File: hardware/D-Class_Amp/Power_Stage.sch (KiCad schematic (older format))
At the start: 19 parts, among them Q301 PHP23NQ11T, Q302 PHP23NQ11T, Q303 PHP23NQ11T, Q304 PHP23NQ11T, U301 NCP1117-12_TO252, U302 IR21834, U303 IR21834

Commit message: foot
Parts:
- R301, R302, R303, R304, R305, R306: footprint (none) -> Resistor_SMD:R_0805_2012Metric_Pad1.20x1.40mm_HandSolder
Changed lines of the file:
@@
 Non-Inverting Half-Bridge\n
-$Comp
-L Device:R R305
-U 1 1 610540BF
-P 5350 1800
-F 0 "R305" V 5143 1800 50  0000 C CNN
-F 1 "10" V 5234 1800 50  0000 C CNN
-F 2 "" V 5280 1800 50  0001 C CNN
-F 3 "~" H 5350 1800 50  0001 C CNN
-	1    5350 1800
-	0    1    1    0
-$EndComp
-$Comp
-L Device:R R301
-U 1 1 61051377
-P 5350 1300
-F 0 "R301" V 5143 1300 50  0000 C CNN
-F 1 "10" V 5234 1300 50  0000 C CNN
-F 2 "" V 5280 1300 50  0001 C CNN
-F 3 "~" H 5350 1300 50  0001 C CNN
-	1    5350 1300
-	0    1    1    0
-$EndComp
 $Comp
 L Device:R R303
@@
 F 0 "R303" V 3650 1700 50  0000 C CNN
 F 1 "10k" V 3550 1700 50  0000 C CNN
-F 2 "" V 3680 1700 50  0001 C CNN
+F 2 "Resistor_SMD:R_0805_2012Metric_Pad1.20x1.40mm_HandSolder" V 3680 1700 50  0001 C CNN
 F 3 "~" H 3750 1700 50  0001 C CNN
 	1    3750 1700
@@
 F 0 "R302" V 8643 1300 50  0000 C CNN
 F 1 "10" V 8734 1300 50  0000 C CNN
-F 2 "" V 8780 1300 50  0001 C CNN
+F 2 "Resistor_SMD:R_0805_2012Metric_Pad1.20x1.40mm_HandSolder" V 8780 1300 50  0001 C CNN
 F 3 "~" H 8850 1300 50  0001 C CNN
 	1    8850 1300
@@
 F 0 "R304" V 10350 1700 50  0000 C CNN
 F 1 "10k" V 10250 1700 50  0000 C CNN
-F 2 "" V 10380 1700 50  0001 C CNN
+F 2 "Resistor_SMD:R_0805_2012Metric_Pad1.20x1.40mm_HandSolder" V 10380 1700 50  0001 C CNN
 F 3 "~" H 10450 1700 50  0001 C CNN
 	1    10450 1700
@@
 F 0 "R306" V 8643 1800 50  0000 C CNN
 F 1 "10" V 8734 1800 50  0000 C CNN
-F 2 "" V 8780 1800 50  0001 C CNN
+F 2 "Resistor_SMD:R_0805_2012Metric_Pad1.20x1.40mm_HandSolder" V 8780 1800 50  0001 C CNN
 F 3 "~" H 8850 1800 50  0001 C CNN
 	1    8850 1800
@@
 Wire Wire Line
 	1300 1750 1750 1750
+$Comp
+L Device:R R305
+U 1 1 610540BF
+P 5350 1800
+F 0 "R305" V 5143 1800 50  0000 C CNN
+F 1 "10" V 5234 1800 50  0000 C CNN
+F 2 "Resistor_SMD:R_0805_2012Metric_Pad1.20x1.40mm_HandSolder" V 5280 1800 50  0001 C CNN
+F 3 "~" H 5350 1800 50  0001 C CNN
+	1    5350 1800
+	0    1    1    0
+$EndComp
+$Comp
+L Device:R R301
+U 1 1 61051377
+P 5350 1300
+F 0 "R301" V 5143 1300 50  0000 C CNN
+F 1 "10" V 5234 1300 50  0000 C CNN
+F 2 "Resistor_SMD:R_0805_2012Metric_Pad1.20x1.40mm_HandSolder" V 5280 1300 50  0001 C CNN
+F 3 "~" H 5350 1300 50  0001 C CNN
+	1    5350 1300
+	0    1    1    0
+$EndComp
 $EndSCHEMATC

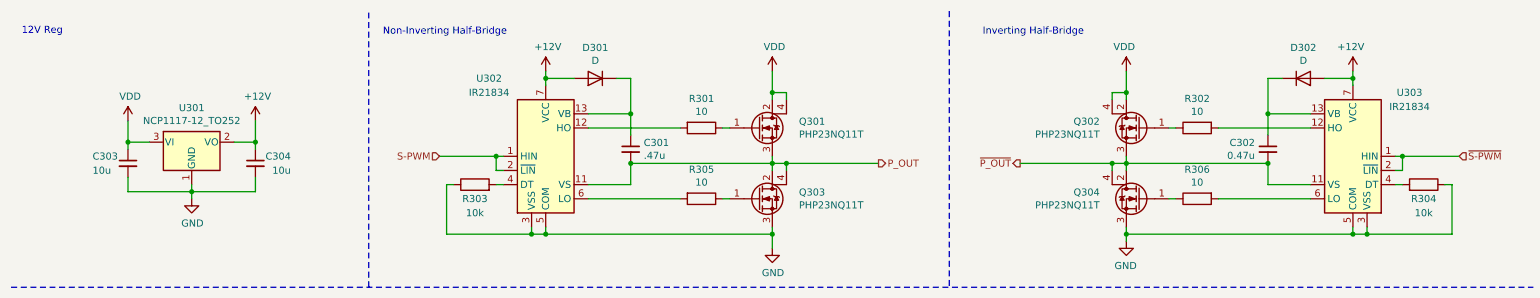
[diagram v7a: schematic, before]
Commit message: footed ic
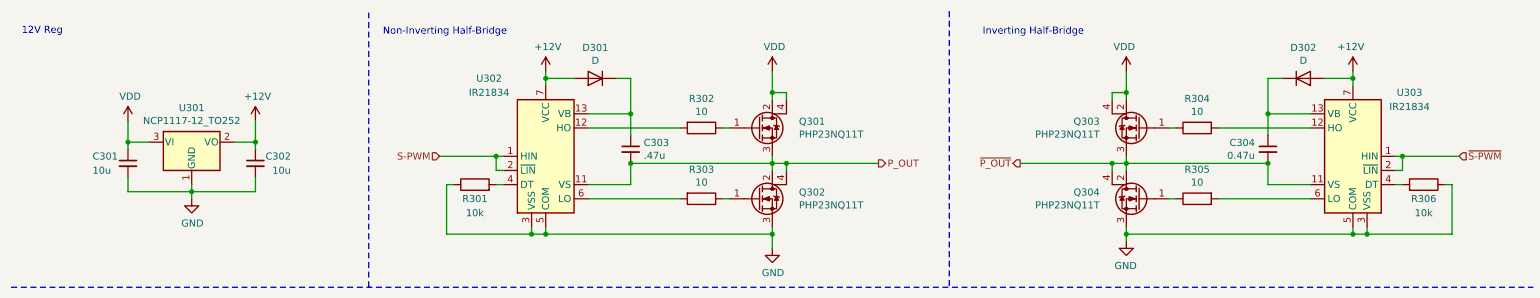
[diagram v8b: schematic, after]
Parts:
- C301: renamed from C303; footprint (none) -> Capacitor_SMD:C_0805_2012Metric_Pad1.18x1.45mm_HandSolder
- C302: renamed from C304; footprint (none) -> Capacitor_SMD:C_0805_2012Metric_Pad1.18x1.45mm_HandSolder
- C303: renamed from C301; footprint (none) -> Capacitor_SMD:C_0805_2012Metric_Pad1.18x1.45mm_HandSolder
- C304: renamed from C302; footprint (none) -> Capacitor_SMD:C_0805_2012Metric_Pad1.18x1.45mm_HandSolder
- Q301, Q304: footprint (none) -> Package_TO_SOT_THT:TO-220-3_Vertical
- Q302: renamed from Q303; footprint (none) -> Package_TO_SOT_THT:TO-220-3_Vertical
- Q303: renamed from Q302; footprint (none) -> Package_TO_SOT_THT:TO-220-3_Vertical
- U302, U303: footprint (none) -> Package_SO:SOIC-14_3.9x8.7mm_P1.27mm
- renumbered R303 to R301, R301 to R302, R305 to R303, R302 to R304, R306 to R305, R304 to R306
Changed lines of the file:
@@
 $EndDescr
 $Comp
-L power:VDD #PWR0302
+L power:VDD #PWR0305
 U 1 1 6105D8A1
 P 5850 900
-F 0 "#PWR0302" H 5850 750 50  0001 C CNN
+F 0 "#PWR0305" H 5850 750 50  0001 C CNN
 F 1 "VDD" H 5865 1073 50  0000 C CNN
 F 2 "" H 5850 900 50  0001 C CNN
@@
 S-PWM
 $Comp
-L Device:C_Small C301
+L Device:C_Small C303
 U 1 1 610A4CCB
 P 4850 1450
-F 0 "C301" H 4942 1496 50  0000 L CNN
+F 0 "C303" H 4942 1496 50  0000 L CNN
 F 1 ".47u" H 4942 1405 50  0000 L CNN
-F 2 "" H 4850 1450 50  0001 C CNN
+F 2 "Capacitor_SMD:C_0805_2012Metric_Pad1.18x1.45mm_HandSolder" H 4850 1450 50  0001 C CNN
 F 3 "~" H 4850 1450 50  0001 C CNN
 	1    4850 1450
@@
 $EndComp
 $Comp
-L power:+12V #PWR0301
+L power:+12V #PWR0304
 U 1 1 610ABD74
 P 4250 900
-F 0 "#PWR0301" H 4250 750 50  0001 C CNN
+F 0 "#PWR0304" H 4250 750 50  0001 C CNN
 F 1 "+12V" H 4265 1073 50  0000 C CNN
 F 2 "" H 4250 900 50  0001 C CNN
@@
 Non-Inverting Half-Bridge\n
 $Comp
-L Device:R R303
+L Device:R R301
 U 1 1 61055141
 P 3750 1700
-F 0 "R303" V 3650 1700 50  0000 C CNN
+F 0 "R301" V 3650 1700 50  0000 C CNN
 F 1 "10k" V 3550 1700 50  0000 C CNN
 F 2 "Resistor_SMD:R_0805_2012Metric_Pad1.20x1.40mm_HandSolder" V 3680 1700 50  0001 C CNN
@@
 $EndComp
 $Comp
-L Device:Q_NMOS_GDSD Q303
+L Device:Q_NMOS_GDSD Q302
 U 1 1 6104F394
 P 5750 1800
-F 0 "Q303" H 6038 1846 50  0000 L CNN
+F 0 "Q302" H 6038 1846 50  0000 L CNN
 F 1 "PHP23NQ11T" H 6038 1755 50  0000 L CNN
-F 2 "" H 5950 1900 50  0001 C CNN
+F 2 "Package_TO_SOT_THT:TO-220-3_Vertical" H 5950 1900 50  0001 C CNN
 F 3 "https://assets.nexperia.com/documents/data-sheet/PHP23NQ11T.pdf" H 5750 1800 50  0001 C CNN
 	1    5750 1800
@@
 F 0 "Q301" H 6038 1346 50  0000 L CNN
 F 1 "PHP23NQ11T" H 6038 1255 50  0000 L CNN
-F 2 "" H 5950 1400 50  0001 C CNN
+F 2 "Package_TO_SOT_THT:TO-220-3_Vertical" H 5950 1400 50  0001 C CNN
 F 3 "https://assets.nexperia.com/documents/data-sheet/PHP23NQ11T.pdf" H 5750 1300 50  0001 C CNN
 	1    5750 1300
@@
 F 0 "U302" H 3850 2050 50  0000 C CNN
 F 1 "IR21834" H 3850 1950 50  0000 C CNN
-F 2 "" H 4250 1500 50  0001 C CIN
+F 2 "Package_SO:SOIC-14_3.9x8.7mm_P1.27mm" H 4250 1500 50  0001 C CIN
 F 3 "https://www.infineon.com/dgdl/ir2183.pdf?fileId=5546d462533600a4015355c9490e16d1" H 4250 1500 50  0001 C CNN
 	1    4250 1500
@@
 $EndComp
 $Comp
-L power:GND #PWR0309
+L power:GND #PWR0306
 U 1 1 6107E9DB
 P 5850 2150
-F 0 "#PWR0309" H 5850 1900 50  0001 C CNN
+F 0 "#PWR0306" H 5850 1900 50  0001 C CNN
 F 1 "GND" H 5855 1977 50  0000 C CNN
 F 2 "" H 5850 2150 50  0001 C CNN
@@
 $EndComp
 $Comp
-L Device:Q_NMOS_GDSD Q302
+L Device:Q_NMOS_GDSD Q303
 U 1 1 610F221C
 P 8450 1300
-F 0 "Q302" H 8738 1346 50  0000 L CNN
+F 0 "Q303" H 8738 1346 50  0000 L CNN
 F 1 "PHP23NQ11T" H 8738 1255 50  0000 L CNN
-F 2 "" H 8650 1400 50  0001 C CNN
+F 2 "Package_TO_SOT_THT:TO-220-3_Vertical" H 8650 1400 50  0001 C CNN
 F 3 "https://assets.nexperia.com/documents/data-sheet/PHP23NQ11T.pdf" H 8450 1300 50  0001 C CNN
 	1    8450 1300
@@
 F 0 "Q304" H 8738 1846 50  0000 L CNN
 F 1 "PHP23NQ11T" H 8738 1755 50  0000 L CNN
-F 2 "" H 8650 1900 50  0001 C CNN
+F 2 "Package_TO_SOT_THT:TO-220-3_Vertical" H 8650 1900 50  0001 C CNN
 F 3 "https://assets.nexperia.com/documents/data-sheet/PHP23NQ11T.pdf" H 8450 1800 50  0001 C CNN
 	1    8450 1800
@@
 F 0 "U303" H 9550 1950 50  0000 C CNN
 F 1 "IR21834" H 9550 1850 50  0000 C CNN
-F 2 "" H 9950 1500 50  0001 C CIN
+F 2 "Package_SO:SOIC-14_3.9x8.7mm_P1.27mm" H 9950 1500 50  0001 C CIN
 F 3 "https://www.infineon.com/dgdl/ir2183.pdf?fileId=5546d462533600a4015355c9490e16d1" H 9950 1500 50  0001 C CNN
 	1    9950 1500
@@
 $EndComp
 $Comp
-L Device:R R302
+L Device:R R304
 U 1 1 610F2230
 P 8850 1300
-F 0 "R302" V 8643 1300 50  0000 C CNN
+F 0 "R304" V 8643 1300 50  0000 C CNN
 F 1 "10" V 8734 1300 50  0000 C CNN
 F 2 "Resistor_SMD:R_0805_2012Metric_Pad1.20x1.40mm_HandSolder" V 8780 1300 50  0001 C CNN
@@
 	10700 1500 10300 1500
 $Comp
-L power:+12V #PWR0304
+L power:+12V #PWR0309
 U 1 1 610F2278
 P 9950 900
-F 0 "#PWR0304" H 9950 750 50  0001 C CNN
+F 0 "#PWR0309" H 9950 750 50  0001 C CNN
 F 1 "+12V" H 9965 1073 50  0000 C CNN
 F 2 "" H 9950 900 50  0001 C CNN
@@
 $EndComp
 $Comp
-L Device:C_Small C302
+L Device:C_Small C304
 U 1 1 610F226E
 P 9350 1450
-F 0 "C302" H 9442 1496 50  0000 L CNN
+F 0 "C304" H 9442 1496 50  0000 L CNN
 F 1 "0.47u" H 9442 1405 50  0000 L CNN
-F 2 "" H 9350 1450 50  0001 C CNN
+F 2 "Capacitor_SMD:C_0805_2012Metric_Pad1.18x1.45mm_HandSolder" H 9350 1450 50  0001 C CNN
 F 3 "~" H 9350 1450 50  0001 C CNN
 	1    9350 1450
@@
 $EndComp
 $Comp
-L power:VDD #PWR0303
+L power:VDD #PWR0307
 U 1 1 610F224E
 P 8350 900
-F 0 "#PWR0303" H 8350 750 50  0001 C CNN
+F 0 "#PWR0307" H 8350 750 50  0001 C CNN
 F 1 "VDD" H 8365 1073 50  0000 C CNN
 F 2 "" H 8350 900 50  0001 C CNN
@@
 $EndComp
 $Comp
-L Device:R R304
+L Device:R R306
 U 1 1 610F2244
 P 10450 1700
-F 0 "R304" V 10350 1700 50  0000 C CNN
+F 0 "R306" V 10350 1700 50  0000 C CNN
 F 1 "10k" V 10250 1700 50  0000 C CNN
 F 2 "Resistor_SMD:R_0805_2012Metric_Pad1.20x1.40mm_HandSolder" V 10380 1700 50  0001 C CNN
@@
 $EndComp
 $Comp
-L Device:R R306
+L Device:R R305
 U 1 1 610F223A
 P 8850 1800
-F 0 "R306" V 8643 1800 50  0000 C CNN
+F 0 "R305" V 8643 1800 50  0000 C CNN
 F 1 "10" V 8734 1800 50  0000 C CNN
 F 2 "Resistor_SMD:R_0805_2012Metric_Pad1.20x1.40mm_HandSolder" V 8780 1800 50  0001 C CNN
@@
 $EndComp
 $Comp
-L power:+12V #PWR0306
+L power:+12V #PWR0303
 U 1 1 61106009
 P 2200 1250
-F 0 "#PWR0306" H 2200 1100 50  0001 C CNN
+F 0 "#PWR0303" H 2200 1100 50  0001 C CNN
 F 1 "+12V" H 2215 1423 50  0000 C CNN
 F 2 "" H 2200 1250 50  0001 C CNN
@@
 $EndComp
 $Comp
-L power:VDD #PWR0305
+L power:VDD #PWR0301
 U 1 1 61109C5A
 P 1300 1250
-F 0 "#PWR0305" H 1300 1100 50  0001 C CNN
+F 0 "#PWR0301" H 1300 1100 50  0001 C CNN
 F 1 "VDD" H 1315 1423 50  0000 C CNN
 F 2 "" H 1300 1250 50  0001 C CNN
@@
 $EndComp
 $Comp
-L power:GND #PWR0307
+L power:GND #PWR0302
 U 1 1 6110DE87
 P 1750 1800
-F 0 "#PWR0307" H 1750 1550 50  0001 C CNN
+F 0 "#PWR0302" H 1750 1550 50  0001 C CNN
 F 1 "GND" H 1755 1627 50  0000 C CNN
 F 2 "" H 1750 1800 50  0001 C CNN
@@
 	1300 1650 1300 1750
 $Comp
-L Device:C_Small C303
+L Device:C_Small C301
 U 1 1 6116A646
 P 1300 1550
-F 0 "C303" H 1050 1600 50  0000 L CNN
+F 0 "C301" H 1050 1600 50  0000 L CNN
 F 1 "10u" H 1050 1500 50  0000 L CNN
-F 2 "" H 1300 1550 50  0001 C CNN
+F 2 "Capacitor_SMD:C_0805_2012Metric_Pad1.18x1.45mm_HandSolder" H 1300 1550 50  0001 C CNN
 F 3 "~" H 1300 1550 50  0001 C CNN
 	1    1300 1550
@@
 $EndComp
 $Comp
-L Device:C_Small C304
+L Device:C_Small C302
 U 1 1 6116D137
 P 2200 1550
-F 0 "C304" H 1950 1600 50  0000 L CNN
+F 0 "C302" H 1950 1600 50  0000 L CNN
 F 1 "10u" H 1950 1500 50  0000 L CNN
-F 2 "" H 2200 1550 50  0001 C CNN
+F 2 "Capacitor_SMD:C_0805_2012Metric_Pad1.18x1.45mm_HandSolder" H 2200 1550 50  0001 C CNN
 F 3 "~" H 2200 1550 50  0001 C CNN
 	1    2200 1550
@@
 	1300 1750 1750 1750
 $Comp
-L Device:R R305
+L Device:R R303
 U 1 1 610540BF
 P 5350 1800
-F 0 "R305" V 5143 1800 50  0000 C CNN
+F 0 "R303" V 5143 1800 50  0000 C CNN
 F 1 "10" V 5234 1800 50  0000 C CNN
 F 2 "Resistor_SMD:R_0805_2012Metric_Pad1.20x1.40mm_HandSolder" V 5280 1800 50  0001 C CNN
@@
 $EndComp
 $Comp
-L Device:R R301
+L Device:R R302
 U 1 1 61051377
 P 5350 1300
-F 0 "R301" V 5143 1300 50  0000 C CNN
+F 0 "R302" V 5143 1300 50  0000 C CNN
 F 1 "10" V 5234 1300 50  0000 C CNN
 F 2 "Resistor_SMD:R_0805_2012Metric_Pad1.20x1.40mm_HandSolder" V 5280 1300 50  0001 C CNN
